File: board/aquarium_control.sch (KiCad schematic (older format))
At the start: 9 parts, among them J1 Barrel_Jack, U1 AP1507

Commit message: Finished power supply design (hopefully)
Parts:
- added F1: Fuse, symbol Fuse
- added R1, R2: R, symbol R
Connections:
- net +5V: now also R1.2; no longer U1.4 (FB)
- net GND: now also R2.1
- net at C1.1, C2.1, U1.1 (Vin): now also F1.1; no longer J1.1
- new net: R1.1, R2.2, U1.4 (FB)
- new net VD: F1.2, J1.1
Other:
- moved on the sheet: C1, C2, C3, C4, D1, J1, L3, U1

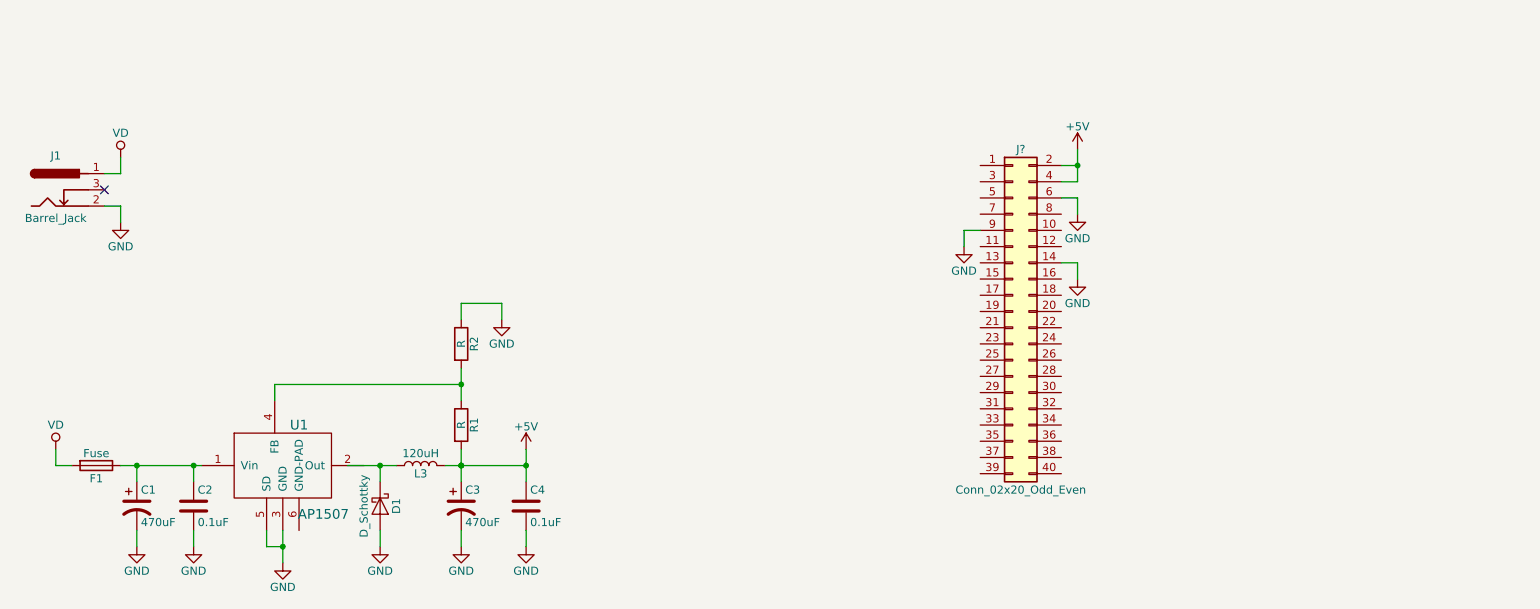
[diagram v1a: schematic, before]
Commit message: First draft of the board schematic
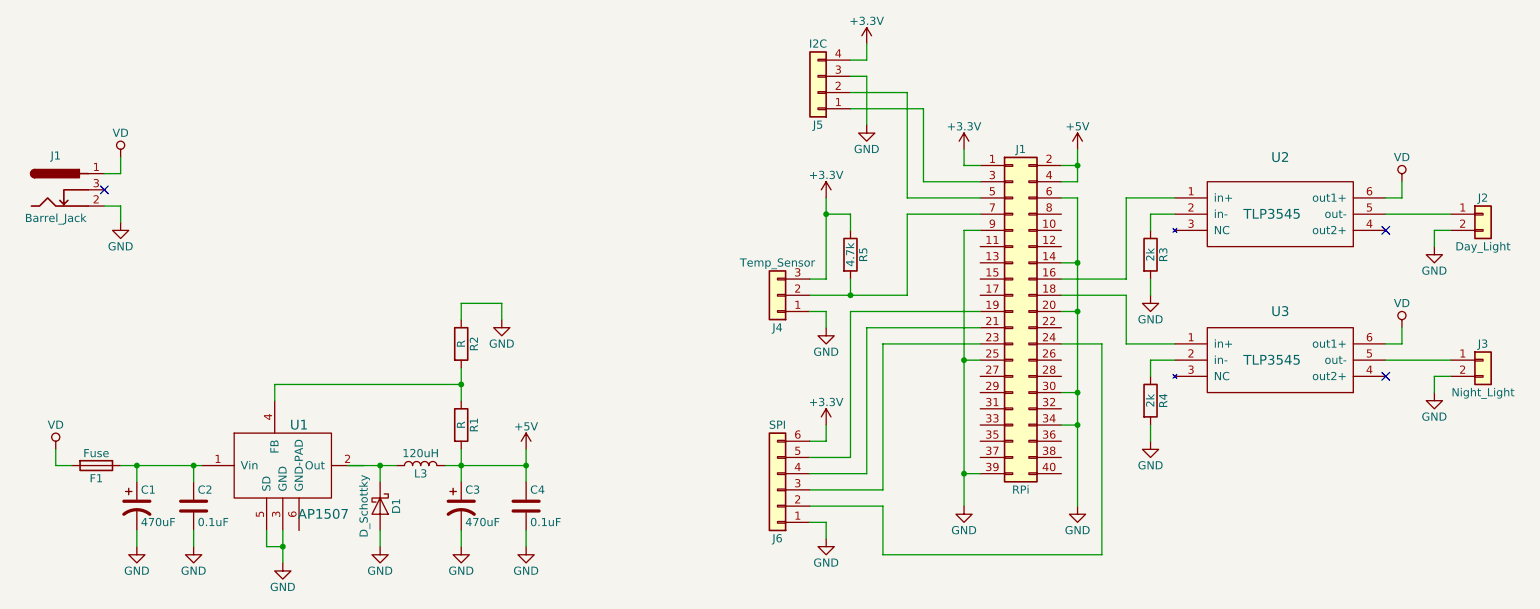
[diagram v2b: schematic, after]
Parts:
- added J2: Day_Light, symbol Conn_01x02
- added J3: Night_Light, symbol Conn_01x02
- added J4: Temp_Sensor, symbol Conn_01x03
- added J5: I2C, symbol Conn_01x04
- added J6: SPI, symbol Conn_01x06
- added R3, R4: 2k, symbol R
- added R5: 4.7k, symbol R
- added U2, U3: TLP3545, symbol TLP3545
- J1: renamed from J?; value Conn_02x20_Odd_Even -> RPi
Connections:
- net GND: now also J1.20 (Pin_20), J1.25 (Pin_25), J1.30 (Pin_30), J1.34 (Pin_34), J1.39 (Pin_39), J2.2 (Pin_2), J3.2 (Pin_2), J4.1 (Pin_1), J5.3 (Pin_3), J6.1 (Pin_1), R3.2, R4.2
- net VD: now also U2.6 (out1+), U3.6 (out1+)
- net +3V3: now reaches J1.1 (Pin_1)
- net +3V3: now also J4.3 (Pin_3), J5.4 (Pin_4), J6.6 (Pin_6), R5.1
- net at J1.16 (Pin_16): now also U2.1 (in+)
- net at J1.18 (Pin_18): now also U3.1 (in+)
- net at J1.19 (Pin_19): now also J6.5 (Pin_5)
- net at J1.21 (Pin_21): now also J6.4 (Pin_4)
- net at J1.23 (Pin_23): now also J6.3 (Pin_3)
- net at J1.24 (Pin_24): now also J6.2 (Pin_2)
- net at J1.3 (Pin_3): now also J5.1 (Pin_1)
- net at J1.5 (Pin_5): now also J5.2 (Pin_2)
- net at J1.7 (Pin_7): now also J4.2 (Pin_2), R5.2
- new net: R3.1, U2.2 (in-)
- new net: J2.1 (Pin_1), U2.5 (out-)
- new net: R4.1, U3.2 (in-)
- new net: J3.1 (Pin_1), U3.5 (out-)
- no-connect marks 1 -> 3

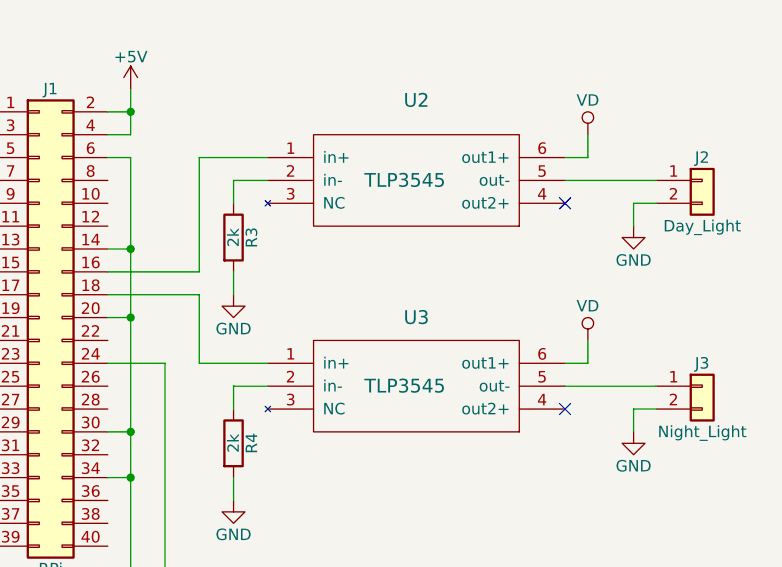
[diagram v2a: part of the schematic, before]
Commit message: Reorganized and split up components
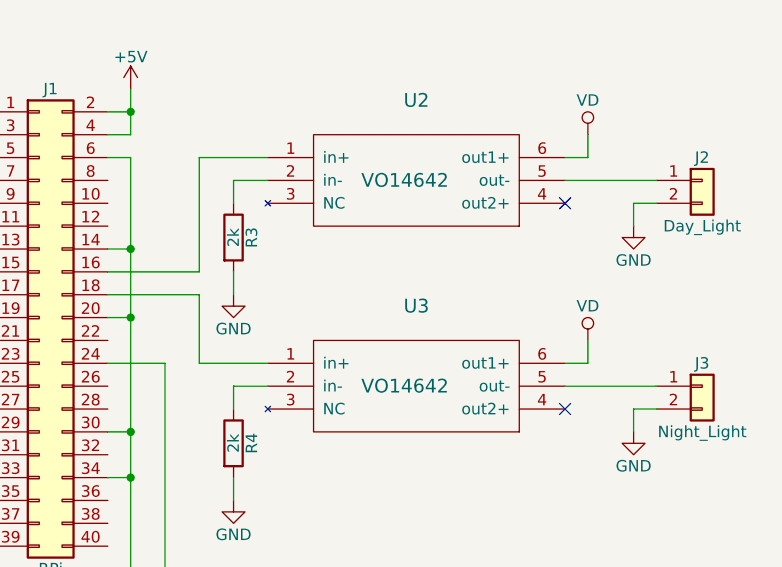
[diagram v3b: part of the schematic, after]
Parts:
- removed U2, U3: TLP3545, symbol TLP3545
- added U2, U3: VO14642, symbol VO14642
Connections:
- net VD: now also U2.6 (out1+), U3.6 (out1+)
- net at J1.16 (Pin_16): now also U2.1 (in+)
- net at J1.18 (Pin_18): now also U3.1 (in+)
- net at R3.1: now also U2.2 (in-)
- net at J2.1 (Pin_1): now also U2.5 (out-)
- net at R4.1: now also U3.2 (in-)
- net at J3.1 (Pin_1): now also U3.5 (out-)
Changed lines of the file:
@@
 LIBS:contrib
 LIBS:valves
-LIBS:ap1507
-LIBS:tlp3545
+LIBS:AP1507
+LIBS:VO14642
 LIBS:aquarium_control-cache
 EELAYER 25 0
@@
 	4250 3250 4250 3350
 $Comp
-L TLP3545 U2
-U 1 1 59CAB4E0
-P 9050 2750
-F 0 "U2" H 9050 3150 60  0000 C CNN
-F 1 "TLP3545" H 9000 2800 60  0000 C CNN
-F 2 "" H 9050 2750 60  0001 C CNN
-F 3 "" H 9050 2750 60  0001 C CNN
-	1    9050 2750
-	1    0    0    -1
-$EndComp
-$Comp
-L TLP3545 U3
-U 1 1 59CAB531
-P 9050 3650
-F 0 "U3" H 9050 4000 60  0000 C CNN
-F 1 "TLP3545" H 9000 3700 60  0000 C CNN
-F 2 "" H 9050 3650 60  0001 C CNN
-F 3 "" H 9050 3650 60  0001 C CNN
-	1    9050 3650
-	1    0    0    -1
-$EndComp
-$Comp
 L R R3
 U 1 1 59CAB78A
@@
 Wire Wire Line
 	6600 4500 6150 4500
+$Comp
+L VO14642 U2
+U 1 1 59CB2CCA
+P 9050 2750
+F 0 "U2" H 9050 3150 60  0000 C CNN
+F 1 "VO14642" H 9000 2800 60  0000 C CNN
+F 2 "" H 9050 2750 60  0001 C CNN
+F 3 "" H 9050 2750 60  0001 C CNN
+	1    9050 2750
+	1    0    0    -1
+$EndComp
+$Comp
+L VO14642 U3
+U 1 1 59CB2D99
+P 9050 3650
+F 0 "U3" H 9050 4050 60  0000 C CNN
+F 1 "VO14642" H 9000 3700 60  0000 C CNN
+F 2 "" H 9050 3650 60  0001 C CNN
+F 3 "" H 9050 3650 60  0001 C CNN
+	1    9050 3650
+	1    0    0    -1
+$EndComp
 $EndSCHEMATC

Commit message: Moved project components into a submodule
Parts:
- C1: footprint (none) -> Capacitors_SMD:CP_Elec_10x10
- C2, C4: footprint (none) -> Capacitors_SMD:C_0805_HandSoldering
- C3: footprint (none) -> Capacitors_SMD:CP_Elec_8x10
- F1: footprint (none) -> Resistors_SMD:R_1206_HandSoldering
- J2, J3: footprint (none) -> Pin_Headers:Pin_Header_Straight_1x02_Pitch2.54mm
- J4: footprint (none) -> Pin_Headers:Pin_Header_Straight_1x03_Pitch2.54mm
- J5: value I2C -> LCD; footprint (none) -> Pin_Headers:Pin_Header_Straight_1x04_Pitch2.54mm
- J6: footprint (none) -> Pin_Headers:Pin_Header_Straight_1x06_Pitch2.54mm
- R1, R2, R3, R4, R5: footprint (none) -> Resistors_SMD:R_0805_HandSoldering
- U1: footprint (none) -> TO_SOT_Packages_SMD:TO-252-5_TabPin6
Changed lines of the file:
@@
 F 0 "U1" H 3000 4200 60  0000 C CNN
 F 1 "AP1507" H 3150 3650 60  0000 C CNN
-F 2 "" H 2950 4100 60  0001 C CNN
+F 2 "TO_SOT_Packages_SMD:TO-252-5_TabPin6" H 2950 4100 60  0001 C CNN
 F 3 "" H 2950 4100 60  0001 C CNN
 	1    2950 4100
@@
 F 0 "C3" H 4025 4600 50  0000 L CNN
 F 1 "470uF" H 4025 4400 50  0000 L CNN
-F 2 "" H 4000 4500 50  0001 C CNN
+F 2 "Capacitors_SMD:CP_Elec_8x10" H 4000 4500 50  0001 C CNN
 F 3 "" H 4000 4500 50  0001 C CNN
 	1    4000 4500
@@
 F 0 "C1" H 2025 4600 50  0000 L CNN
 F 1 "470uF" H 2025 4400 50  0000 L CNN
-F 2 "" H 2000 4500 50  0001 C CNN
+F 2 "Capacitors_SMD:CP_Elec_10x10" H 2000 4500 50  0001 C CNN
 F 3 "" H 2000 4500 50  0001 C CNN
 	1    2000 4500
@@
 F 0 "C2" H 2375 4600 50  0000 L CNN
 F 1 "0.1uF" H 2375 4400 50  0000 L CNN
-F 2 "" H 2388 4350 50  0001 C CNN
+F 2 "Capacitors_SMD:C_0805_HandSoldering" H 2388 4350 50  0001 C CNN
 F 3 "" H 2350 4500 50  0001 C CNN
 	1    2350 4500
@@
 F 0 "C4" H 4425 4600 50  0000 L CNN
 F 1 "0.1uF" H 4425 4400 50  0000 L CNN
-F 2 "" H 4438 4350 50  0001 C CNN
+F 2 "Capacitors_SMD:C_0805_HandSoldering" H 4438 4350 50  0001 C CNN
 F 3 "" H 4400 4500 50  0001 C CNN
 	1    4400 4500
@@
 F 0 "F1" V 1830 4250 50  0000 C CNN
 F 1 "Fuse" V 1675 4250 50  0000 C CNN
-F 2 "" V 1680 4250 50  0001 C CNN
+F 2 "Resistors_SMD:R_1206_HandSoldering" V 1680 4250 50  0001 C CNN
 F 3 "" H 1750 4250 50  0001 C CNN
 	1    1750 4250
@@
 F 0 "R1" V 4080 4000 50  0000 C CNN
 F 1 "R" V 4000 4000 50  0000 C CNN
-F 2 "" V 3930 4000 50  0001 C CNN
+F 2 "Resistors_SMD:R_0805_HandSoldering" V 3930 4000 50  0001 C CNN
 F 3 "" H 4000 4000 50  0001 C CNN
 	1    4000 4000
@@
 F 0 "R2" V 4080 3500 50  0000 C CNN
 F 1 "R" V 4000 3500 50  0000 C CNN
-F 2 "" V 3930 3500 50  0001 C CNN
+F 2 "Resistors_SMD:R_0805_HandSoldering" V 3930 3500 50  0001 C CNN
 F 3 "" H 4000 3500 50  0001 C CNN
 	1    4000 3500
@@
 F 0 "R3" V 8330 2950 50  0000 C CNN
 F 1 "2k" V 8250 2950 50  0000 C CNN
-F 2 "" V 8180 2950 50  0001 C CNN
+F 2 "Resistors_SMD:R_0805_HandSoldering" V 8180 2950 50  0001 C CNN
 F 3 "" H 8250 2950 50  0001 C CNN
 	1    8250 2950
@@
 F 0 "R4" V 8330 3850 50  0000 C CNN
 F 1 "2k" V 8250 3850 50  0000 C CNN
-F 2 "" V 8180 3850 50  0001 C CNN
+F 2 "Resistors_SMD:R_0805_HandSoldering" V 8180 3850 50  0001 C CNN
 F 3 "" H 8250 3850 50  0001 C CNN
 	1    8250 3850
@@
 F 0 "J2" H 10300 2800 50  0000 C CNN
 F 1 "Day_Light" H 10300 2500 50  0000 C CNN
-F 2 "" H 10300 2700 50  0001 C CNN
+F 2 "Pin_Headers:Pin_Header_Straight_1x02_Pitch2.54mm" H 10300 2700 50  0001 C CNN
 F 3 "" H 10300 2700 50  0001 C CNN
 	1    10300 2700
@@
 F 0 "J3" H 10300 3700 50  0000 C CNN
 F 1 "Night_Light" H 10300 3400 50  0000 C CNN
-F 2 "" H 10300 3600 50  0001 C CNN
+F 2 "Pin_Headers:Pin_Header_Straight_1x02_Pitch2.54mm" H 10300 3600 50  0001 C CNN
 F 3 "" H 10300 3600 50  0001 C CNN
 	1    10300 3600
@@
 F 0 "J4" H 5950 3400 50  0000 C CNN
 F 1 "Temp_Sensor" H 5950 3000 50  0000 C CNN
-F 2 "" H 5950 3200 50  0001 C CNN
+F 2 "Pin_Headers:Pin_Header_Straight_1x03_Pitch2.54mm" H 5950 3200 50  0001 C CNN
 F 3 "" H 5950 3200 50  0001 C CNN
 	1    5950 3200
@@
 F 0 "R5" V 6480 2950 50  0000 C CNN
 F 1 "4.7k" V 6400 2950 50  0000 C CNN
-F 2 "" V 6330 2950 50  0001 C CNN
+F 2 "Resistors_SMD:R_0805_HandSoldering" V 6330 2950 50  0001 C CNN
 F 3 "" H 6400 2950 50  0001 C CNN
 	1    6400 2950
@@
 P 6200 1950
 F 0 "J5" H 6200 2150 50  0000 C CNN
-F 1 "I2C" H 6200 1650 50  0000 C CNN
-F 2 "" H 6200 1950 50  0001 C CNN
+F 1 "LCD" H 6200 1650 50  0000 C CNN
+F 2 "Pin_Headers:Pin_Header_Straight_1x04_Pitch2.54mm" H 6200 1950 50  0001 C CNN
 F 3 "" H 6200 1950 50  0001 C CNN
 	1    6200 1950
@@
 F 0 "J6" H 5950 4700 50  0000 C CNN
 F 1 "SPI" H 5950 4000 50  0000 C CNN
-F 2 "" H 5950 4400 50  0001 C CNN
+F 2 "Pin_Headers:Pin_Header_Straight_1x06_Pitch2.54mm" H 5950 4400 50  0001 C CNN
 F 3 "" H 5950 4400 50  0001 C CNN
 	1    5950 4400

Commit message: Swapped out components to use new centralized parts repo
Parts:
- U1: footprint TO_SOT_Packages_SMD:TO-252-5_TabPin6 -> (none)
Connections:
- net at J1.16 (Pin_16): now also U3.1 (in+); no longer U2.1 (in+)
- net at J1.18 (Pin_18): now also U2.1 (in+); no longer U3.1 (in+)
- net at R3.1: now also U3.2 (in-); no longer U2.2 (in-)
- net at R4.1: now also U2.2 (in-); no longer U3.2 (in-)
- net at J2.1 (Pin_1): now also U3.5 (out-); no longer U2.5 (out-)
- net at J3.1 (Pin_1): now also U2.5 (out-); no longer U3.5 (out-)
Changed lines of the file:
@@
 LIBS:contrib
 LIBS:valves
-LIBS:AP1507
-LIBS:VO14642
+LIBS:nebrius-lcd
+LIBS:nebrius-regulators
+LIBS:nebrius-switch
 LIBS:aquarium_control-cache
 EELAYER 25 0
@@
 	1    0    0    -1
 $EndComp
-$Comp
-L AP1507 U1
-U 1 1 59C89407
-P 2950 4100
-F 0 "U1" H 3000 4200 60  0000 C CNN
-F 1 "AP1507" H 3150 3650 60  0000 C CNN
-F 2 "TO_SOT_Packages_SMD:TO-252-5_TabPin6" H 2950 4100 60  0001 C CNN
-F 3 "" H 2950 4100 60  0001 C CNN
-	1    2950 4100
-	1    0    0    -1
-$EndComp
 Wire Wire Line
 	1900 4250 2400 4250
@@
 	6600 4500 6150 4500
 $Comp
-L VO14642 U2
-U 1 1 59CB2CCA
+L AP1507 U1
+U 1 1 5A189BEF
+P 2950 4100
+F 0 "U1" H 3000 4200 60  0000 C CNN
+F 1 "AP1507" H 3150 3650 60  0000 C CNN
+F 2 "" H 2950 4100 60  0001 C CNN
+F 3 "" H 2950 4100 60  0001 C CNN
+	1    2950 4100
+	1    0    0    -1
+$EndComp
+$Comp
+L VO14642 U3
+U 1 1 5A189F0E
 P 9050 2750
-F 0 "U2" H 9050 3150 60  0000 C CNN
+F 0 "U3" H 9050 3150 60  0000 C CNN
 F 1 "VO14642" H 9000 2800 60  0000 C CNN
 F 2 "" H 9050 2750 60  0001 C CNN
@@
 $EndComp
 $Comp
-L VO14642 U3
-U 1 1 59CB2D99
+L VO14642 U2
+U 1 1 5A189F8D
 P 9050 3650
-F 0 "U3" H 9050 4050 60  0000 C CNN
+F 0 "U2" H 9050 4050 60  0000 C CNN
 F 1 "VO14642" H 9000 3700 60  0000 C CNN
 F 2 "" H 9050 3650 60  0001 C CNN

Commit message: Updates to the board
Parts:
- added J7: Fan, Pin_Headers:Pin_Header_Straight_1x02_Pitch2.54mm, symbol Conn_01x02
- U1: footprint (none) -> nebrius-regulator:AP1507
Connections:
- net GND: now also U1.6 (GND-PAD), J7.2 (Pin_2)
- net VD: now also J7.1 (Pin_1)
- net at D1.1 (K), L3.1: now also U1.2 (Out)
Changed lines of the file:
@@
 	2800 4650 2800 4750
 Wire Wire Line
-	2800 4750 2900 4750
+	2800 4750 3000 4750
 Connection ~ 2900 4750
 $Comp
@@
 $EndComp
 Wire Wire Line
-	3300 4250 3600 4250
-Wire Wire Line
 	3500 4250 3500 4350
 $Comp
@@
 	6600 4500 6150 4500
 $Comp
-L AP1507 U1
-U 1 1 5A189BEF
-P 2950 4100
-F 0 "U1" H 3000 4200 60  0000 C CNN
-F 1 "AP1507" H 3150 3650 60  0000 C CNN
-F 2 "" H 2950 4100 60  0001 C CNN
-F 3 "" H 2950 4100 60  0001 C CNN
-	1    2950 4100
-	1    0    0    -1
-$EndComp
-$Comp
 L VO14642 U3
 U 1 1 5A189F0E
@@
 	1    0    0    -1
 $EndComp
+$Comp
+L AP1507 U1
+U 1 1 5A18C3F5
+P 2950 4100
+F 0 "U1" H 3000 4200 60  0000 C CNN
+F 1 "AP1507" H 2600 4300 60  0000 C CNN
+F 2 "nebrius-regulator:AP1507" H 2950 4100 60  0001 C CNN
+F 3 "" H 2950 4100 60  0001 C CNN
+	1    2950 4100
+	1    0    0    -1
+$EndComp
+Wire Wire Line
+	3000 4750 3000 4650
+$Comp
+L Conn_01x02 J7
+U 1 1 5A18C694
+P 3350 2400
+F 0 "J7" H 3350 2500 50  0000 C CNN
+F 1 "Fan" H 3350 2200 50  0000 C CNN
+F 2 "Pin_Headers:Pin_Header_Straight_1x02_Pitch2.54mm" H 3350 2400 50  0001 C CNN
+F 3 "" H 3350 2400 50  0001 C CNN
+	1    3350 2400
+	1    0    0    -1
+$EndComp
+$Comp
+L GND #PWR?
+U 1 1 5A18C7C8
+P 3050 2600
+F 0 "#PWR?" H 3050 2350 50  0001 C CNN
+F 1 "GND" H 3050 2450 50  0000 C CNN
+F 2 "" H 3050 2600 50  0001 C CNN
+F 3 "" H 3050 2600 50  0001 C CNN
+	1    3050 2600
+	1    0    0    -1
+$EndComp
+$Comp
+L VD #PWR?
+U 1 1 5A18C838
+P 3050 2300
+F 0 "#PWR?" H 3050 2150 50  0001 C CNN
+F 1 "VD" H 3050 2450 50  0000 C CNN
+F 2 "" H 3050 2300 50  0001 C CNN
+F 3 "" H 3050 2300 50  0001 C CNN
+	1    3050 2300
+	1    0    0    -1
+$EndComp
+Wire Wire Line
+	3050 2300 3050 2400
+Wire Wire Line
+	3050 2400 3150 2400
+Wire Wire Line
+	3150 2500 3050 2500
+Wire Wire Line
+	3050 2500 3050 2600
+Wire Wire Line
+	3400 4250 3600 4250
 $EndSCHEMATC
